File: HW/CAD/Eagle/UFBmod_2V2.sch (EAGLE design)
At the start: 200 parts, among them J1411 ABRACON_ARJE-0034, T0551 MMBT2222, U0501 MIDAS_MCCOG21605B6W-FPTLWI, U0601 MAX5217, U0701 AT86RF215-ZU, U0711 ASVTX-13-D-26.000MHZ-I05-T, U0811 PE4259, U0821 RFX1010, U0881 B39871B3440U410, U0911 FT232HL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

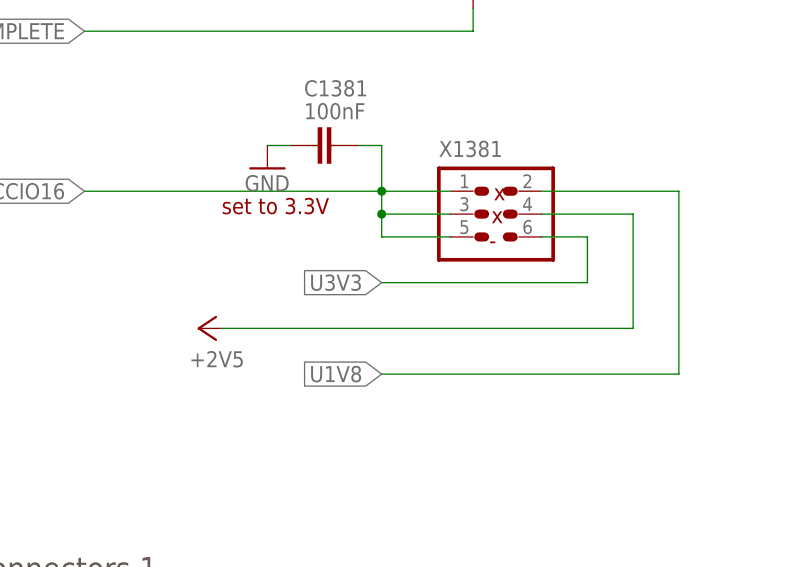
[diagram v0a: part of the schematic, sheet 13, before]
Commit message: HW - Eagle - V2.2 - inductor sizes fixed
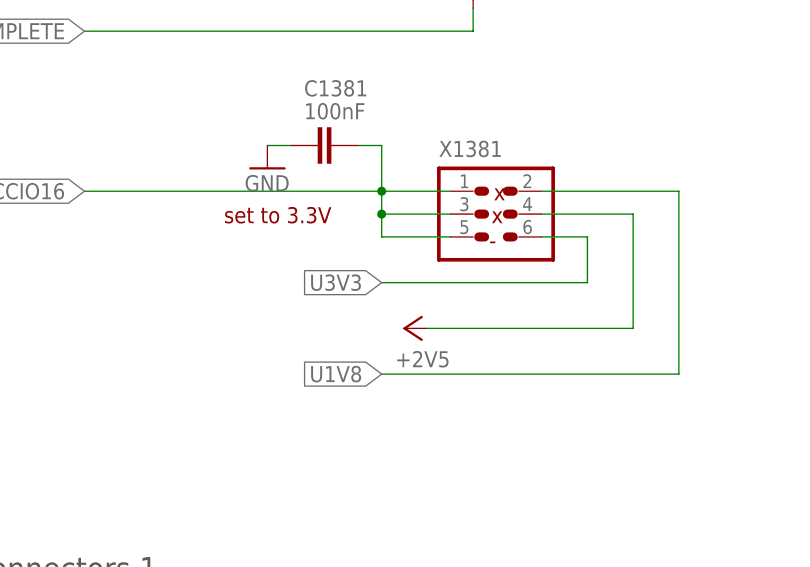
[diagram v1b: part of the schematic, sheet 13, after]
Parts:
- L1101: value 440nH -> 470nH; device df4iah_rcl:L-EUL1812 -> df4iah_rcl:L-EUL5650M
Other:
- note added: "MURATA DFE252010P-4R7M=P2 2.50 mm x 2.00 mm"
- note added: "PULSE PA5003.471NLT (470 nH, 18.4 A, 4.13 mR) 5.50 mm x 5.30 mm"
- note removed: "MURATA DFE252010P-4R7M=P2"
- note removed: "PULSE PA0513.441NL"
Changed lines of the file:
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@@
 <part name="H1514" library="df4iah_holes" deviceset="MOUNT-PAD-ROUND" device="3.2" value="MOUNT-PAD-ROUND3.2"/>
 <part name="GND1514" library="df4iah_supply" deviceset="GND" device=""/>
-<part name="L1101" library="df4iah_rcl" deviceset="L-EU" device="L1812" value="440nH"/>
+<part name="L1101" library="df4iah_rcl" deviceset="L-EU" device="L5650M" value="470nH"/>
 <part name="GND1121" library="df4iah_supply" deviceset="GND" device=""/>
 <part name="C1153" library="df4iah_rcl" deviceset="C-EU" device="C0805" value="100uF"/>
@@
 <text x="22.86" y="162.56" size="2.54" layer="97" ratio="15">PMIC 5V..14V --&gt; 3.3V_REG</text>
 <text x="165.1" y="15.24" size="2.54" layer="97" ratio="15">PMIC: 5V..14V --&gt; 3.3V</text>
-<text x="165.1" y="116.84" size="1.778" layer="97">PULSE PA0513.441NL</text>
-<text x="165.1" y="122.174" size="1.778" layer="97">(Better: 1uH .. 1.5 uH)</text>
+<text x="160.02" y="109.22" size="1.778" layer="97">PULSE PA5003.471NLT (470 nH, 18.4 A, 4.13 mR)
+5.50 mm x 5.30 mm</text>
+<text x="160.02" y="117.094" size="1.778" layer="97">(Better: 1uH .. 1.5 uH)</text>
 <text x="139.7" y="134.62" size="1.778" layer="97" rot="R90">25V</text>
 <text x="134.62" y="134.62" size="1.778" layer="97" rot="R90">25V</text>
@@
 <text x="22.86" y="162.56" size="2.54" layer="97" ratio="15">PMIC 3.5V --&gt; 2.5V</text>
 <text x="165.1" y="15.24" size="2.54" layer="97" ratio="15">PMIC: 3.5V --&gt; 2.5V</text>
-<text x="149.86" y="119.38" size="1.778" layer="97">MURATA DFE252010P-4R7M=P2</text>
+<text x="149.86" y="119.38" size="1.778" layer="97">MURATA DFE252010P-4R7M=P2
+2.50 mm x 2.00 mm
+</text>
 <text x="96.52" y="78.74" size="1.778" layer="97" rot="R90">Prog: 2.5V</text>
 <text x="132.08" y="116.84" size="1.778" layer="97">300mA</text>
@@
 <text x="15.24" y="96.52" size="1.778" layer="97">Programmer:
 Digilent JTAG HS3</text>
-<text x="193.04" y="55.88" size="1.778" layer="94">set to 3.3V</text>
+<text x="193.294" y="54.864" size="1.778" layer="94">set to 3.3V</text>
 <text x="223.266" y="57.404" size="1.778" layer="94">x</text>
 <text x="223.012" y="54.864" size="1.778" layer="94">x</text>
@@
 <instance part="R1366" gate="G$1" x="236.22" y="129.54"/>
 <instance part="X1381" gate="G$1" x="223.52" y="55.88"/>
-<instance part="+2V5_1350" gate="G$2" x="190.5" y="43.18" rot="R90"/>
+<instance part="+2V5_1350" gate="G$2" x="213.36" y="43.18" rot="R90"/>
 <instance part="C1381" gate="G$1" x="203.2" y="63.5" smashed="yes" rot="R90">
 <attribute name="NAME" x="202.184" y="68.961" size="1.778" layer="95"/>
@@
 <wire x1="228.6" y1="55.88" x2="238.76" y2="55.88" width="0.1524" layer="91"/>
 <wire x1="238.76" y1="55.88" x2="238.76" y2="43.18" width="0.1524" layer="91"/>
-<wire x1="238.76" y1="43.18" x2="193.04" y2="43.18" width="0.1524" layer="91"/>
+<wire x1="238.76" y1="43.18" x2="215.9" y2="43.18" width="0.1524" layer="91"/>
 <pinref part="+2V5_1350" gate="G$2" pin="+2V5"/>
 </segment>
